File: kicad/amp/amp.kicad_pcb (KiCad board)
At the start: 2 copper layers, 100 x 85 mm, 112 parts, among them J1 DC 12V IN, J2 IN L-G-R, J3 SPK L, J4 SPK R, Q1001 BC547, Q1002 BC547, Q1003 BC557, Q1004 BD139, Q1005 BD140, Q1006 BC547, Q2001 BC547, Q2002 BC547, Q2003 BC557, Q2004 BD139, Q2005 BD140, Q2006 BC547

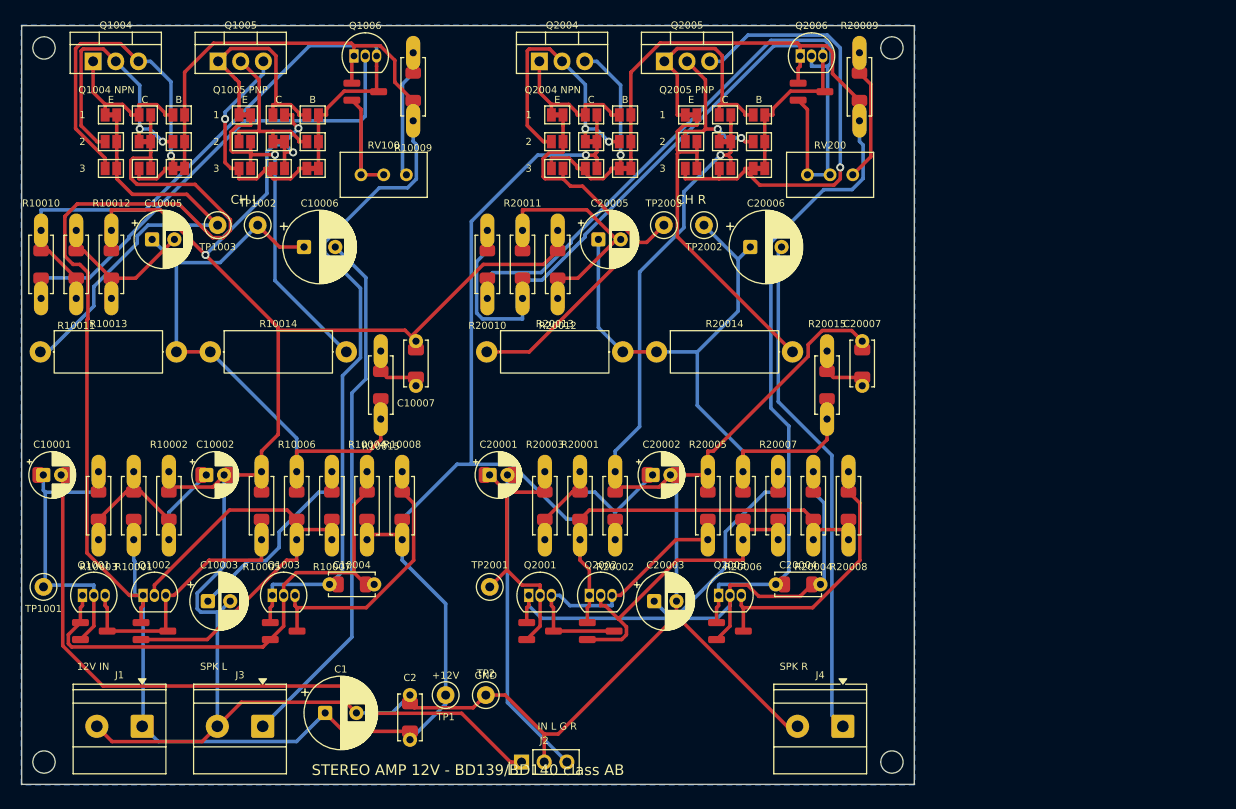
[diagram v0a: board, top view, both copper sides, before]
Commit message: Rotate screw terminals to face the board edge, add 3D views, schematics and layouts to the README, CircuitJS links in the review
Amp board is 100 x 85 mm after the hybrid-footprint courtyards grew; input header moved to open space
on the bottom edge so freerouting completes. Panel 134 x 137 mm, DRC clean.
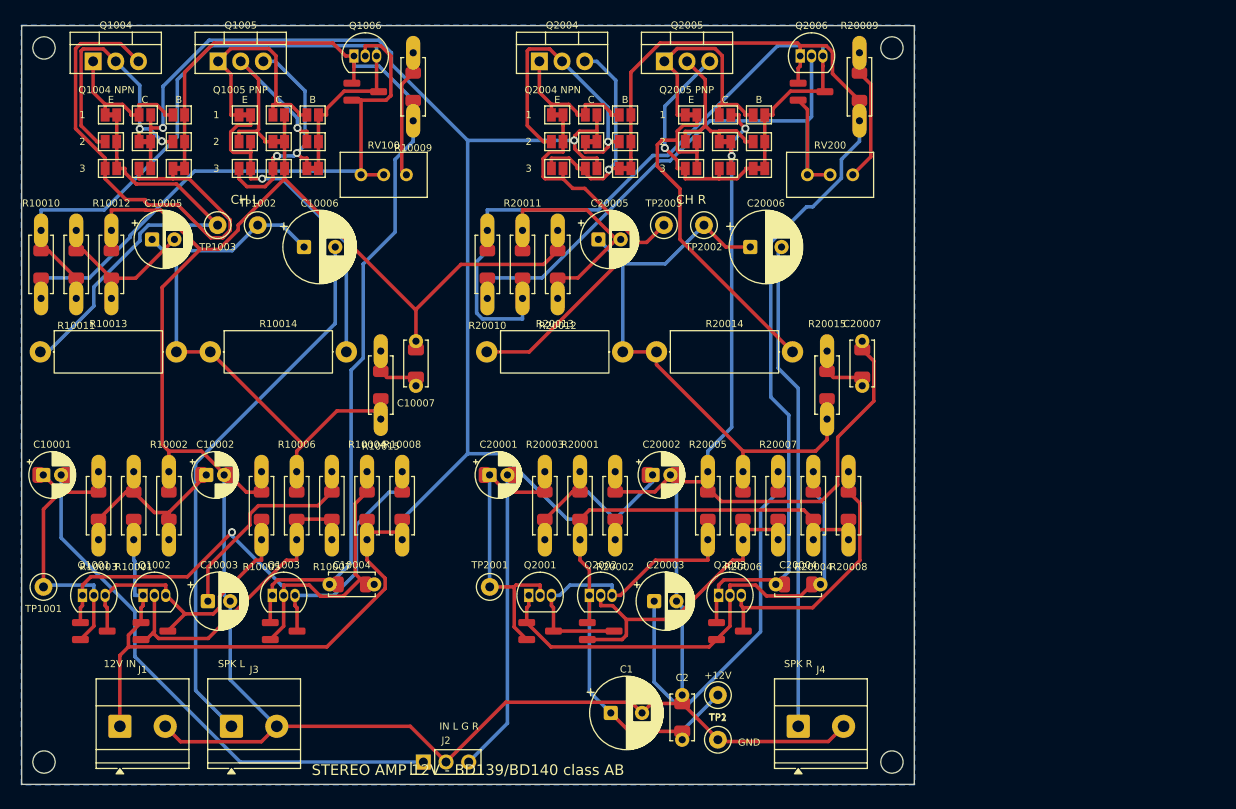
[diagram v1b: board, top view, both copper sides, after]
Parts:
- moved C1 32.0 mm to (116.0, 127.0)
- moved C2 30.5 mm to (124.0, 130.0)
- moved TP1 30.5 mm to (128.0, 125.0)
- moved TP2 26.5 mm to (128.0, 130.0)
- moved J2 11.0 mm to (95.0, 132.5)
- moved J4 5.00 mm to (137.0, 128.5), turned to 0 degrees
- moved J3 3.50 mm to (73.5, 128.5), turned to 0 degrees
- moved J1 2.50 mm to (61.0, 128.5), turned to 0 degrees
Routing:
- net Net-(JP20017-A): track 53.3 -> 26.0 mm
- net +12V: track 316.3 -> 292.3 mm, vias 1 -> 2
- net Net-(C20003-Pad1): track 26.9 -> 46.5 mm
- net Net-(Q1002-B): track 52.9 -> 36.7 mm
- net /IN_L: track 76.5 -> 61.5 mm
- net Net-(JP10007-A): track 42.8 -> 56.9 mm, vias 1 -> 0
- net Net-(Q2006-B): track 83.3 -> 72.5 mm
- net Net-(JP10011-A): track 19.2 -> 26.8 mm, vias 0 -> 1
- net /OUT_R: track 76.3 -> 68.8 mm
- net Net-(Q1001-C): track 59.1 -> 64.4 mm, vias 0 -> 1
- net /VAS_L: track 121.5 -> 116.8 mm
- net /E5_R: track 38.8 -> 43.0 mm
- net /B5_L: track 76.6 -> 80.4 mm
- net /OUT_L: track 71.2 -> 67.7 mm
- net Net-(Q2001-B): track 32.4 -> 35.8 mm
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
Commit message: Square 144 x 144 mm panel with rails; amp widened to 134 x 71 mm so PSU plus volume board match its width; readable silkscreen
References sit inside resistor, diode and ceramic outlines along the body axis, larger text; electrolytic,
transistor and test-point labels stay beside the part. Hybrid footprints built from the library parts keep
polarity marks. All 2-layer boards, the panel and the single-sided PSU and volume boards are DRC clean.
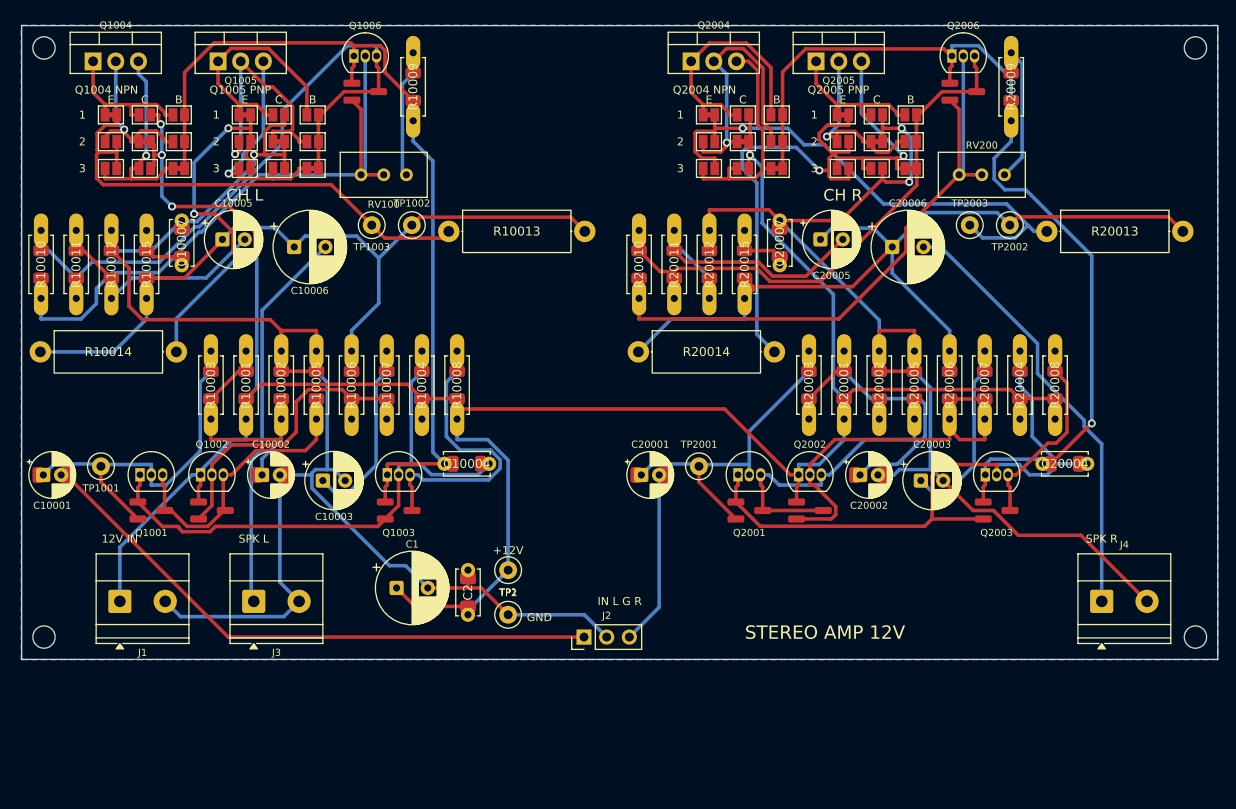
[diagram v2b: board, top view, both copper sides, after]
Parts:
- moved R20013 64.2 mm to (164.8, 73.0)
- moved R10013 47.7 mm to (97.8, 73.0)
- moved H4 36.8 mm to (181.5, 118.5)
- moved J4 36.8 mm to (171.0, 114.5)
- moved TP2002 34.3 mm to (160.7, 72.3)
- moved TP2003 34.3 mm to (156.2, 72.3)
- moved H2 34.0 mm to (181.5, 52.5)
- moved C20003 32.8 mm to (150.7, 101.0)
- moved Q2003 32.8 mm to (158.0, 100.3)
- moved C20004 32.8 mm to (164.4, 99.1)
- moved R20002 32.5 mm to (146.1, 94.1)
- moved R20001 32.5 mm to (142.1, 94.1)
- moved R20003 32.5 mm to (138.2, 94.1)
- moved R10015 29.5 mm to (64.0, 80.6)
- moved C10007 29.5 mm to (67.9, 76.8)
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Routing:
- net GND: track 365.0 -> 305.2 mm, vias 2 -> 3
- net Net-(JP10007-A): track 56.9 -> 24.2 mm, vias 0 -> 1
- net /OUT_R: track 68.8 -> 98.0 mm
- net /B5_R: track 88.9 -> 63.3 mm
- net Net-(C20003-Pad1): track 46.5 -> 23.2 mm
- net /OUT_L: track 67.7 -> 88.4 mm
- net /SPK_L: track 61.8 -> 43.3 mm
- net +12V: track 292.3 -> 274.7 mm, vias 2 -> 5
- net /VAS_L: track 116.8 -> 100.0 mm
- net Net-(Q2001-C): track 59.4 -> 76.0 mm
- net /IN_R: track 34.5 -> 20.1 mm
- net Net-(JP10004-A): track 30.8 -> 19.3 mm, vias 2 -> 1
- net Net-(C20002-Pad1): track 29.0 -> 40.4 mm
- net /E4_R: track 49.3 -> 60.7 mm, vias 0 -> 1
- net Net-(JP20001-A): track 16.5 -> 27.2 mm
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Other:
- board size 100 x 85 mm -> 134 x 71 mm
- board text added: "STEREO AMP 12V"
- board text removed: "STEREO AMP 12V - BD139/BD140 class AB"

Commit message: Repository URL and revision on every silkscreen and on the panel rails
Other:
- board text added: "STEREO AMP 12V v1.0 2026-10"
- board text added: "github.com/lahirunirmalx/discrete-stereo-amp"
- board text removed: "STEREO AMP 12V"
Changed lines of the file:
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@@
+		)
+	)
+	(gr_text "github.com/lahirunirmalx/discrete-stereo-amp"
+		(at 145.95 114.549999 0)
+		(layer "F.SilkS")
+		(effects
+			(font
+				(size 0.9 0.9)
+				(thickness 0.15)
+			)
 		)
 	)
@@
 		)
 	)
-	(gr_text "STEREO AMP 12V"
+	(gr_text "STEREO AMP 12V  v1.0 2026-10"
 		(at 140 118 0)
 		(layer "F.SilkS")

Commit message: Release 1.1: square panel, rotated terminals, readable silkscreen, URL and revision stamps
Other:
- board text added: "STEREO AMP 12V v1.1 2026-10"
- board text removed: "STEREO AMP 12V v1.0 2026-10"
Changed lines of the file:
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@@
 		)
 	)
-	(gr_text "STEREO AMP 12V  v1.0 2026-10"
+	(gr_text "STEREO AMP 12V  v1.1 2026-10"
 		(at 140 118 0)
 		(layer "F.SilkS")

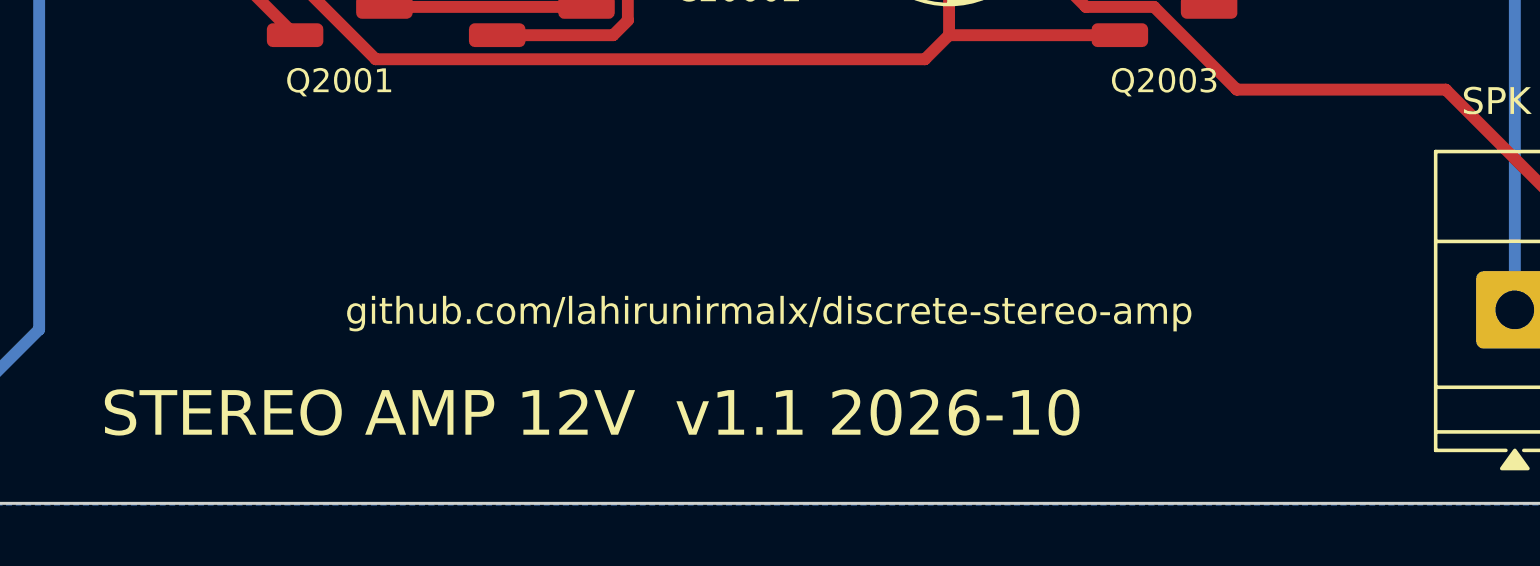
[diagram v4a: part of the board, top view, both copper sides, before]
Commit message: Compact 100 x 85 mm amp layout as a selectable second variant; modular build paths and the three design rules documented; per-board gerbers include both amps
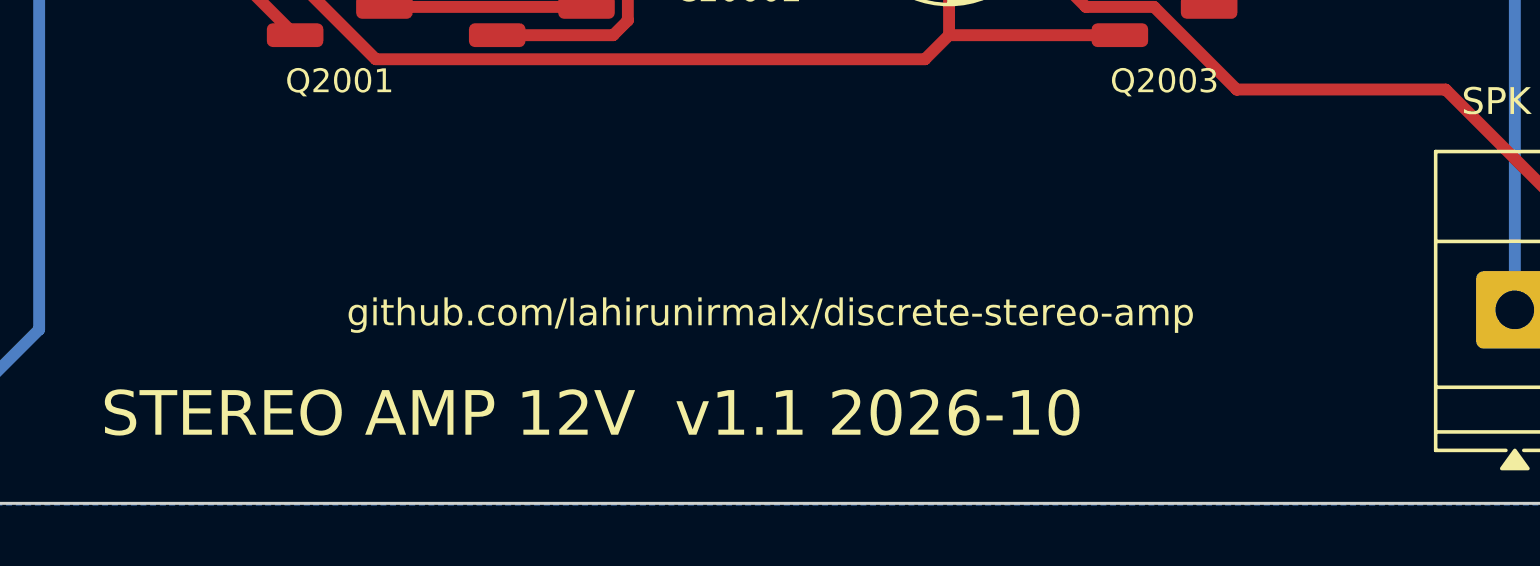
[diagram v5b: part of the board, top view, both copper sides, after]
